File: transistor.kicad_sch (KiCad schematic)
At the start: 4 parts, among them J9 Conn_01x02_Pin, Q1 AO3400A

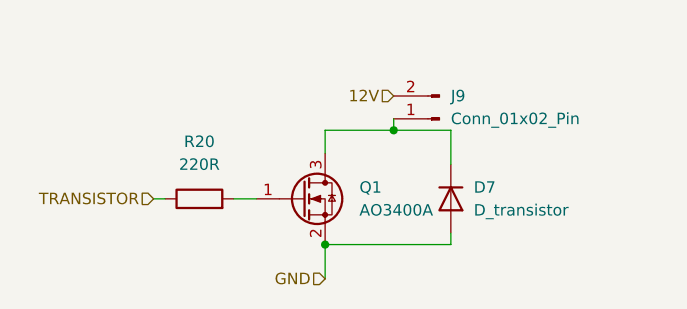
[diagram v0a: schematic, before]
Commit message: fix transistor by adding a correct free-wheeling diode
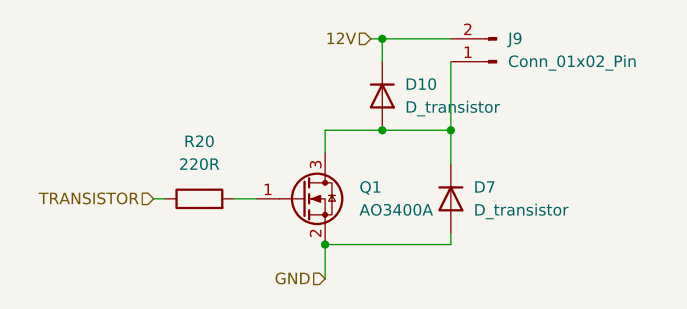
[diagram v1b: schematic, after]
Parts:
- added D10: D_transistor, Diode_SMD:D_SOD-123, symbol Device:D
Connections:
- net 12V: now also D10.1 (K)
- net at D7.1 (K), J9.1 (Pin_1), Q1.3 (D): now also D10.2 (A)
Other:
- moved on the sheet: J9
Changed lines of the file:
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@@
 	(paper "A4")
 	(junction
-		(at 135.89 74.93)
+		(at 134.62 74.93)
 		(diameter 0)
 		(color 0 0 0 0)
@@
 		(color 0 0 0 0)
 	)
+	(junction
+		(at 134.62 64.77)
+		(diameter 0)
+		(color 0 0 0 0)
+	)
+	(junction
+		(at 142.24 74.93)
+		(diameter 0)
+		(color 0 0 0 0)
+	)
 	(wire
 		(pts
@@
 	(wire
 		(pts
+			(xy 134.62 74.93) (xy 142.24 74.93)
+		)
+		(stroke
+			(width 0)
+			(type default)
+		)
+	)
+	(wire
+		(pts
+			(xy 142.24 64.77) (xy 134.62 64.77)
+		)
+		(stroke
+			(width 0)
+			(type default)
+		)
+	)
+	(wire
+		(pts
 			(xy 128.27 74.93) (xy 128.27 77.47)
 		)
@@
 	(wire
 		(pts
+			(xy 134.62 64.77) (xy 133.35 64.77)
+		)
+		(stroke
+			(width 0)
+			(type default)
+		)
+	)
+	(wire
+		(pts
 			(xy 109.22 82.55) (xy 110.49 82.55)
 		)
@@
 	(wire
 		(pts
-			(xy 128.27 74.93) (xy 135.89 74.93)
-		)
-		(stroke
-			(width 0)
-			(type default)
-		)
-	)
-	(wire
-		(pts
-			(xy 135.89 73.66) (xy 135.89 74.93)
+			(xy 128.27 74.93) (xy 134.62 74.93)
+		)
+		(stroke
+			(width 0)
+			(type default)
+		)
+	)
+	(wire
+		(pts
+			(xy 142.24 67.31) (xy 142.24 74.93)
+		)
+		(stroke
+			(width 0)
+			(type default)
+		)
+	)
+	(wire
+		(pts
+			(xy 134.62 64.77) (xy 134.62 67.31)
 		)
 		(stroke
@@
 		(pts
 			(xy 128.27 87.63) (xy 142.24 87.63)
-		)
-		(stroke
-			(width 0)
-			(type default)
-		)
-	)
-	(wire
-		(pts
-			(xy 135.89 74.93) (xy 142.24 74.93)
 		)
 		(stroke
@@
 	(hierarchical_label "12V"
 		(shape input)
-		(at 135.89 71.12 180)
+		(at 133.35 64.77 180)
 		(effects
 			(font
@@
 			)
 			(justify right)
+		)
+	)
+	(symbol
+		(lib_id "Device:D")
+		(at 134.62 71.12 270)
+		(unit 1)
+		(exclude_from_sim no)
+		(in_bom yes)
+		(on_board yes)
+		(dnp no)
+		(fields_autoplaced yes)
+		(property "Reference" "D10"
+			(at 137.16 69.8499 90)
+			(effects
+				(font
+					(size 1.27 1.27)
+				)
+				(justify left)
+			)
+		)
+		(property "Value" "D_transistor"
+			(at 137.16 72.3899 90)
+			(effects
+				(font
+					(size 1.27 1.27)
+				)
+				(justify left)
+			)
+		)
+		(property "Footprint" "Diode_SMD:D_SOD-123"
+			(at 134.62 71.12 0)
+			(effects
+				(font
+					(size 1.27 1.27)
+				)
+				(hide yes)
+			)
+		)
+		(property "Datasheet" "~"
+			(at 134.62 71.12 0)
+			(effects
+				(font
+					(size 1.27 1.27)
+				)
+				(hide yes)
+			)
+		)
+		(property "Description" "Diode"
+			(at 134.62 71.12 0)
+			(effects
+				(font
+					(size 1.27 1.27)
+				)
+				(hide yes)
+			)
+		)
+		(property "LCSC#" "C908230"
+			(at 134.62 71.12 0)
+			(effects
+				(font
+					(size 1.27 1.27)
+				)
+				(hide yes)
+			)
+		)
+		(property "Sim.Device" "D"
+			(at 134.62 71.12 0)
+			(effects
+				(font
+					(size 1.27 1.27)
+				)
+				(hide yes)
+			)
+		)
+		(property "Sim.Pins" "1=K 2=A"
+			(at 134.62 71.12 0)
+			(effects
+				(font
+					(size 1.27 1.27)
+				)
+				(hide yes)
+			)
+		)
+		(pin "1"
+		)
+		(pin "2"
+		)
+		(instances
+			(project "motorBoardCan"
+				(path "/41f25736-b213-4f7f-a532-020d43e6a118/7cd63ed4-9d08-4a3c-b840-01380bea2ccd"
+					(reference "D10")
+					(unit 1)
+				)
+				(path "/41f25736-b213-4f7f-a532-020d43e6a118/7f9f6e98-21bf-497f-b591-15edd85c287f"
+					(reference "D13")
+					(unit 1)
+				)
+				(path "/41f25736-b213-4f7f-a532-020d43e6a118/b5efbc96-45ef-4150-8abb-67059292877d"
+					(reference "D11")
+					(unit 1)
+				)
+				(path "/41f25736-b213-4f7f-a532-020d43e6a118/f360015d-db4b-4b97-b344-ca2e891c0a42"
+					(reference "D12")
+					(unit 1)
+				)
+			)
 		)
 	)
@@
 	(symbol
 		(lib_id "Connector:Conn_01x02_Pin")
-		(at 140.97 73.66 180)
+		(at 147.32 67.31 180)
 		(unit 1)
 		(exclude_from_sim no)
@@
 		(fields_autoplaced yes)
 		(property "Reference" "J9"
-			(at 142.24 71.1199 0)
+			(at 148.59 64.7699 0)
 			(effects
 				(font
@@
 		)
 		(property "Value" "Conn_01x02_Pin"
-			(at 142.24 73.6599 0)
+			(at 148.59 67.3099 0)
 			(effects
 				(font
@@
 		)
 		(property "Footprint" "Connector_JST:JST_XH_B2B-XH-A_1x02_P2.50mm_Vertical"
-			(at 140.97 73.66 0)
+			(at 147.32 67.31 0)
 			(effects
 				(font
@@
 		)
 		(property "Datasheet" "~"
-			(at 140.97 73.66 0)
+			(at 147.32 67.31 0)
 			(effects
 				(font
@@
 		)
 		(property "Description" "Generic connector, single row, 01x02, script generated"
-			(at 140.97 73.66 0)
+			(at 147.32 67.31 0)
 			(effects
 				(font
@@
 		)
 		(property "LCSC#" "C158012"
-			(at 140.97 73.66 0)
-			(effects
-				(font
+			(at 147.32 67.31 0)
+			(effects
+				(font
